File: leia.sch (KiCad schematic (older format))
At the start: 31 parts, among them J1101 TARGET_PWR, J1102 TARGET_GND, J1103 TARGET_EXT_PWR, J1112 TARGET_SHUNT, J6 EXT_READER_VCC, U1001 FOD8001, U520 FOD8012A

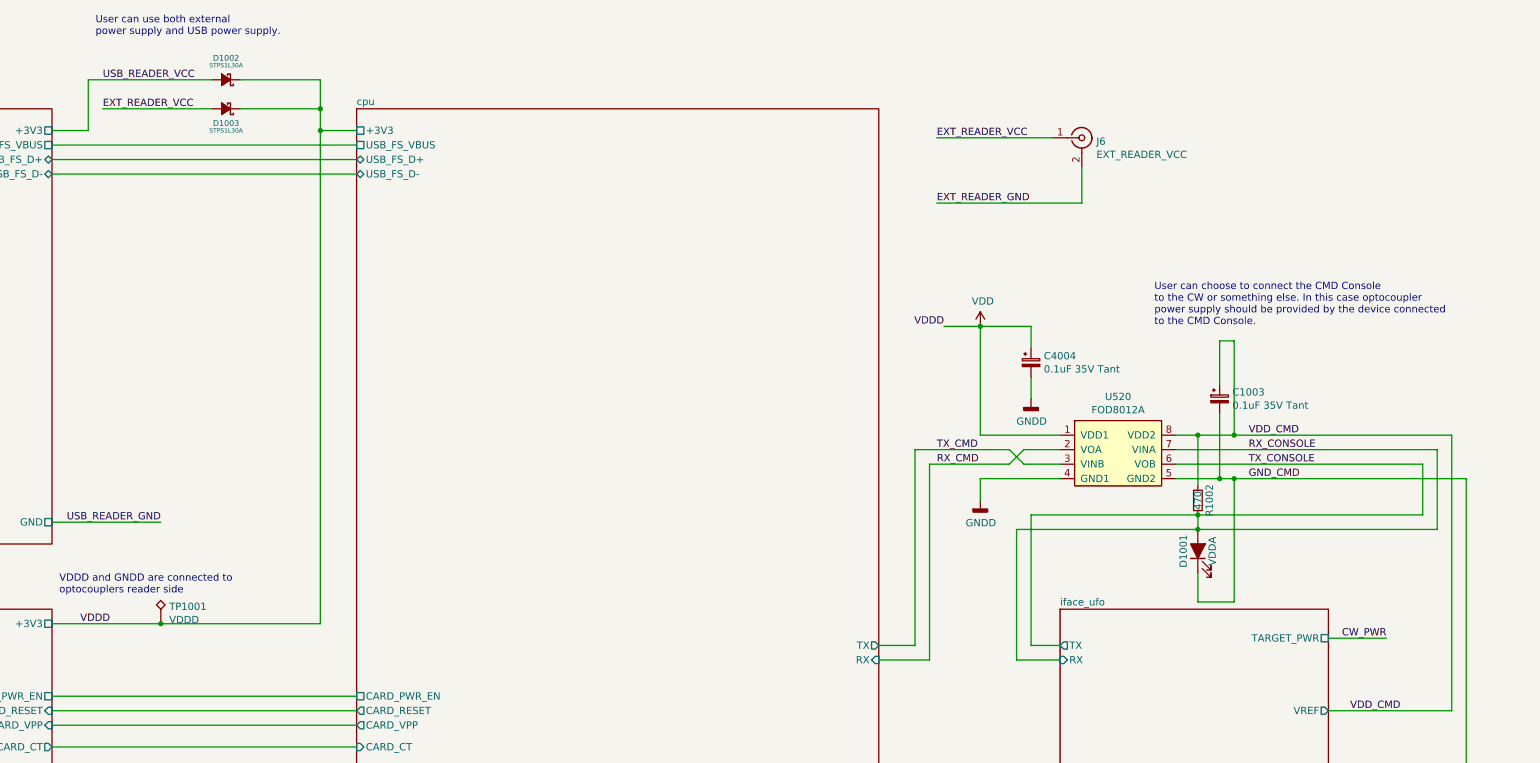
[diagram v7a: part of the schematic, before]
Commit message: [update] switch to Cw 20 pin connector
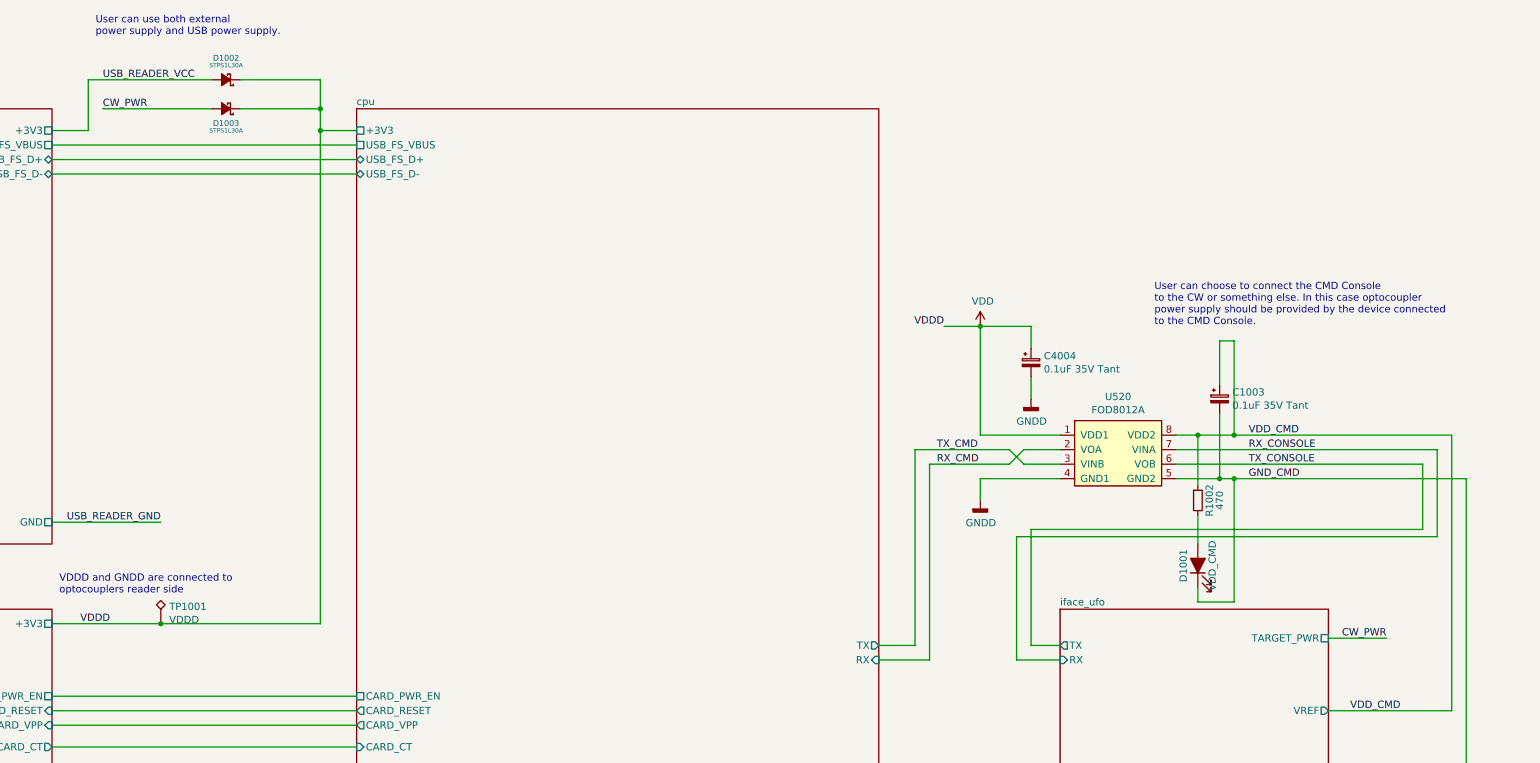
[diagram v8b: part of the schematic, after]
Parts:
- removed J6: EXT_READER_VCC, Connector_Coaxial:SMA_Amphenol_132289_EdgeMount, symbol Connector:Conn_Coaxial
- D1001: value VDDA -> VDD_CMD
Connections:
- net EXT_READER_VCC is gone; now on net CW_PWR: D1003.2 (A)
- net RX_CONSOLE: no longer D1001.2 (A), R1002.2, U520.6 (VOB)
- new net: D1001.2 (A), R1002.2
- new net TX_CONSOLE: U520.6 (VOB)
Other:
- moved on the sheet: D1001
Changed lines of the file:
@@
 Connection ~ 14000 3800
 Connection ~ 13850 3500
-Connection ~ 13850 4050
-Connection ~ 13850 4150
 NoConn ~ 13300 9250
 NoConn ~ 4450 9800
@@
 	12550 3600 12650 3700
 Wire Wire Line
-	12600 4150 12600 5050
-Wire Wire Line
-	12600 4150 13850 4150
+	12600 4200 12600 5050
+Wire Wire Line
+	12600 4200 15500 4200
 Wire Wire Line
 	12600 5050 12900 5050
@@
 	12700 3100 12700 3250
 Wire Wire Line
-	12700 4050 13850 4050
-Wire Wire Line
-	12700 4950 12700 4050
+	12700 4150 15400 4150
+Wire Wire Line
+	12700 4950 12700 4150
 Wire Wire Line
 	12800 8150 12800 8450
 Wire Wire Line
-	12850 1450 12050 1450
-Wire Wire Line
 	12900 3500 12350 3500
 Wire Wire Line
 	12900 4950 12700 4950
 Wire Wire Line
-	13050 1650 13050 1900
-Wire Wire Line
-	13050 1900 12050 1900
-Wire Wire Line
 	13200 7850 12450 7850
 Wire Wire Line
@@
 	13850 3500 14100 3500
 Wire Wire Line
-	13850 4050 13850 4150
-Wire Wire Line
-	13850 4050 15400 4050
-Wire Wire Line
-	13850 4150 15500 4150
-Wire Wire Line
-	13850 4450 13850 4650
+	13850 4050 13850 4250
+Wire Wire Line
+	13850 4550 13850 4650
 Wire Wire Line
 	13850 4650 14100 4650
@@
 	14750 7200 15700 7200
 Wire Wire Line
-	15400 3700 15400 4050
+	15400 3700 15400 4150
 Wire Wire Line
 	15450 6600 15450 8050
 Wire Wire Line
-	15500 4150 15500 3600
+	15500 4200 15500 3600
 Wire Wire Line
 	15600 3500 15600 5400
@@
 USB_READER_VCC
 Text Label 6300 1250 0    50   ~ 0
-EXT_READER_VCC
+CW_PWR
 Text Label 6350 4800 2    50   ~ 0
 VDDD
@@
 Text Label 7300 10100 0    50   ~ 0
 GNDD
-Text Label 12050 1450 0    50   ~ 0
-EXT_READER_VCC
-Text Label 12050 1900 0    50   ~ 0
-EXT_READER_GND
 Text Label 12050 3600 0    50   ~ 0
 TX_CMD
@@
 AR Path="/5CFF7179" Ref="R1002"  Part="1"
 F 0 "R1002" V 13930 3950 50  0000 C CNN
-F 1 "470" V 13850 3950 50  0000 C CNN
+F 1 "470" V 14000 3950 50  0000 C CNN
 F 2 "Resistor_SMD:R_0603_1608Metric" V 13780 3950 30  0001 C CNN
 F 3 "" H 13850 3950 30  0000 C CNN
@@
 L Device:LED_ALT D?
 U 1 1 5CFF716D
-P 13850 4300
+P 13850 4400
 AR Path="/5B22B7CD/5CFF716D" Ref="D?"  Part="1"
 AR Path="/5B19B7B2/5CFF716D" Ref="D?"  Part="1"
 AR Path="/5CBC3017/5B19B7B2/5CFF716D" Ref="D?"  Part="1"
 AR Path="/5CFF716D" Ref="D1001"  Part="1"
-F 0 "D1001" H 13850 4400 50  0000 C CNN
-F 1 "VDDA" H 13850 4200 50  0000 C CNN
-F 2 "LED_SMD:LED_0603_1608Metric_Castellated" H 13850 4300 60  0001 C CNN
-F 3 "" H 13850 4300 60  0000 C CNN
-F 4 "Vishay" H 13850 4300 50  0001 C CNN "MFG Name"
-F 5 "TLMS1100-GS08.." H 13850 4300 50  0001 C CNN "MFG Part Num"
-F 6 "1440338" H 13850 4300 50  0001 C CNN "Distrib PN"
-F 7 "https://fr.farnell.com/vishay/tlms1100-gs08/led-red-1-6mm-x-0-8mm-63mcd-633nm/dp/1440338" H 13850 4300 50  0001 C CNN "Distrib Link"
-F 8 "Farnell" H 13850 4300 50  0001 C CNN "Distrib"
-F 9 "Farnell" H 10350 -1150 50  0001 C CNN "Distrib Name"
-	1    13850 4300
+F 0 "D1001" H 13850 4500 50  0000 C CNN
+F 1 "VDD_CMD" H 13850 4300 50  0000 C CNN
+F 2 "LED_SMD:LED_0603_1608Metric_Castellated" H 13850 4400 60  0001 C CNN
+F 3 "" H 13850 4400 60  0000 C CNN
+F 4 "Vishay" H 13850 4400 50  0001 C CNN "MFG Name"
+F 5 "TLMS1100-GS08.." H 13850 4400 50  0001 C CNN "MFG Part Num"
+F 6 "1440338" H 13850 4400 50  0001 C CNN "Distrib PN"
+F 7 "https://fr.farnell.com/vishay/tlms1100-gs08/led-red-1-6mm-x-0-8mm-63mcd-633nm/dp/1440338" H 13850 4400 50  0001 C CNN "Distrib Link"
+F 8 "Farnell" H 13850 4400 50  0001 C CNN "Distrib"
+F 9 "Farnell" H 10350 -1050 50  0001 C CNN "Distrib Name"
+	1    13850 4400
 	0    -1   -1   0
 $EndComp
@@
 $EndComp
 $Comp
-L Connector:Conn_Coaxial J6
-U 1 1 5C3E3023
-P 13050 1450
-F 0 "J6" H 13150 1425 50  0000 L CNN
-F 1 "EXT_READER_VCC" H 13150 1334 50  0000 L CNN
-F 2 "Connector_Coaxial:SMA_Amphenol_132289_EdgeMount" H 13050 1450 50  0001 C CNN
-F 3 "http://www.farnell.com/datasheets/1681616.pdf" H 13050 1450 50  0001 C CNN
-F 4 "AMPHENOL CONNEX" H 13050 1450 50  0001 C CNN "MFG Name"
-F 5 "132289" H 13050 1450 50  0001 C CNN "MFG Part Num"
-F 6 "Farnell" H 13050 1450 50  0001 C CNN "Distrib"
-F 7 "2112467" H 13050 1450 50  0001 C CNN "Distrib Part Num"
-F 8 "https://fr.farnell.com/amphenol-connex/132289/sma-jack-50ohm-bulkhead/dp/2112467?st=132289" H -1900 -100 50  0001 C CNN "Distrib Link"
-F 9 "Farnell" H -1900 -100 50  0001 C CNN "Distrib Name"
-F 10 "2112467" H -1900 -100 50  0001 C CNN "Distrib PN"
-	1    13050 1450
-	1    0    0    -1
-$EndComp
-$Comp
